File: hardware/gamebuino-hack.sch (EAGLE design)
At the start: 28 parts, among them U1 328P, Y1 16MHz

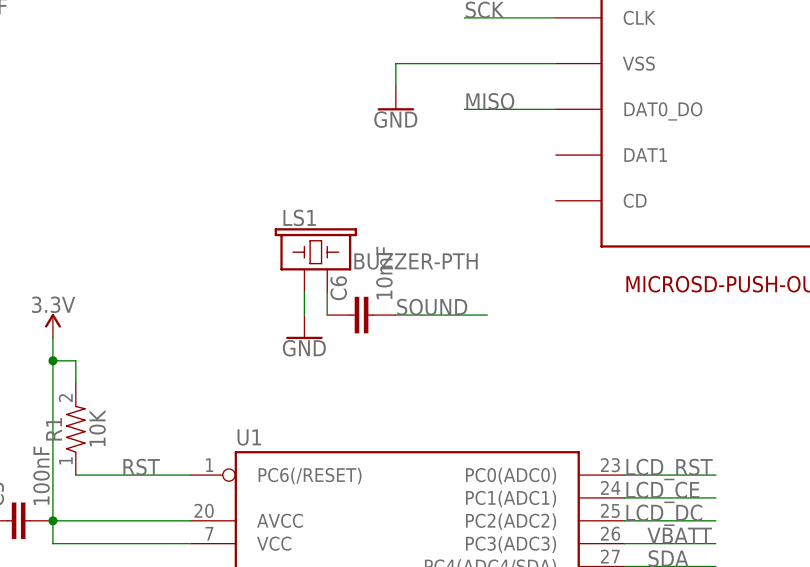
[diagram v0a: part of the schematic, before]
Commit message: Corrected sound output (removed cap)
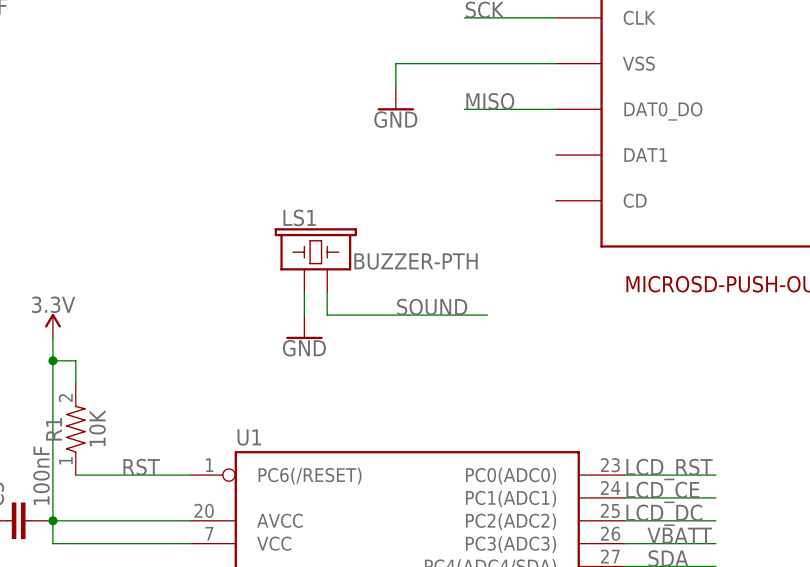
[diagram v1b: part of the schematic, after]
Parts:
- removed C6: 10mF, myParts:CAP-805
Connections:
- removed net N$2: C6.1, LS1.2
- net SOUND: now also LS1.2; no longer C6.2
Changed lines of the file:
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@@
 <part name="GND9" library="SparkFun-PowerSymbols" library_urn="urn:adsk.eagle:library:530" deviceset="GND" device=""/>
 <part name="SUPPLY6" library="SparkFun-PowerSymbols" library_urn="urn:adsk.eagle:library:530" deviceset="VIN" device=""/>
-<part name="C6" library="myParts" deviceset="CAP" device="-805" value="10mF"/>
 <part name="S1" library="SparkFun-Switches" deviceset="SWITCH-SPDT" device="-PTH-11.6X4.0MM"/>
 <part name="SUPPLY1" library="SparkFun-PowerSymbols" deviceset="V_BATT" device=""/>
@@
 <instance part="SUPPLY6" gate="G$1" x="22.86" y="58.42" smashed="yes">
 <attribute name="VALUE" x="22.86" y="61.214" size="1.778" layer="96" align="bottom-center"/>
-</instance>
-<instance part="C6" gate="G$1" x="99.06" y="106.68" smashed="yes" rot="R90">
-<attribute name="NAME" x="96.139" y="108.204" size="1.778" layer="95" font="vector" rot="R90"/>
-<attribute name="VALUE" x="101.219" y="108.204" size="1.778" layer="96" font="vector" rot="R90"/>
 </instance>
 <instance part="S1" gate="1" x="27.94" y="152.4" smashed="yes" rot="R180">
@@
 </segment>
 <segment>
-<pinref part="C6" gate="G$1" pin="2"/>
-<wire x1="101.6" y1="106.68" x2="111.76" y2="106.68" width="0.1524" layer="91"/>
+<wire x1="93.98" y1="106.68" x2="111.76" y2="106.68" width="0.1524" layer="91"/>
 <label x="101.6" y="106.68" size="1.778" layer="95"/>
+<pinref part="LS1" gate="G$1" pin="2"/>
+<wire x1="93.98" y1="109.22" x2="93.98" y2="106.68" width="0.1524" layer="91"/>
 </segment>
 </net>
@@
 </segment>
 </net>
-<net name="N$2" class="0">
-<segment>
-<pinref part="LS1" gate="G$1" pin="2"/>
-<pinref part="C6" gate="G$1" pin="1"/>
-<wire x1="93.98" y1="109.22" x2="93.98" y2="106.68" width="0.1524" layer="91"/>
-</segment>
-</net>
